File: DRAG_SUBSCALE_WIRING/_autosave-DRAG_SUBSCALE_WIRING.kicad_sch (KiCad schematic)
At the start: 7 parts, among them J1 Screw_Terminal_01x02, SW1 SW_DPST_x2, U1 Teensy4.1

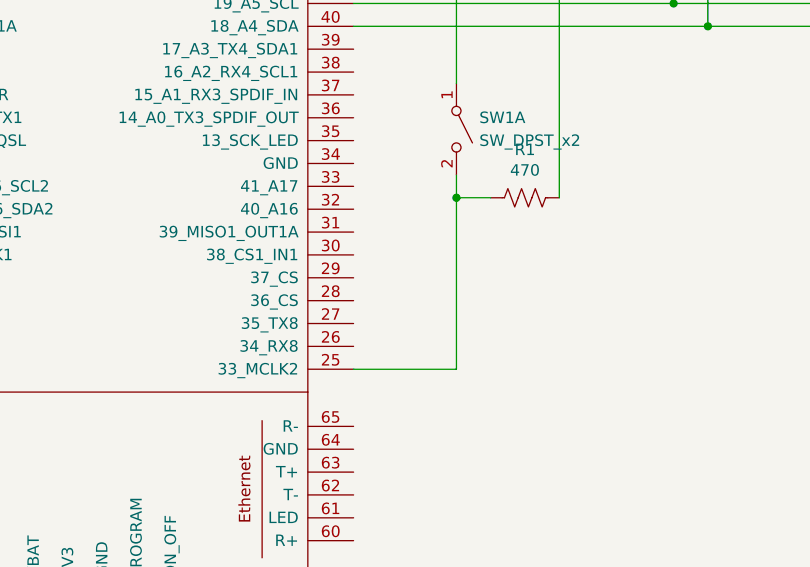
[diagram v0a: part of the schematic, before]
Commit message: Changed buzzer to be more pronounced pitch
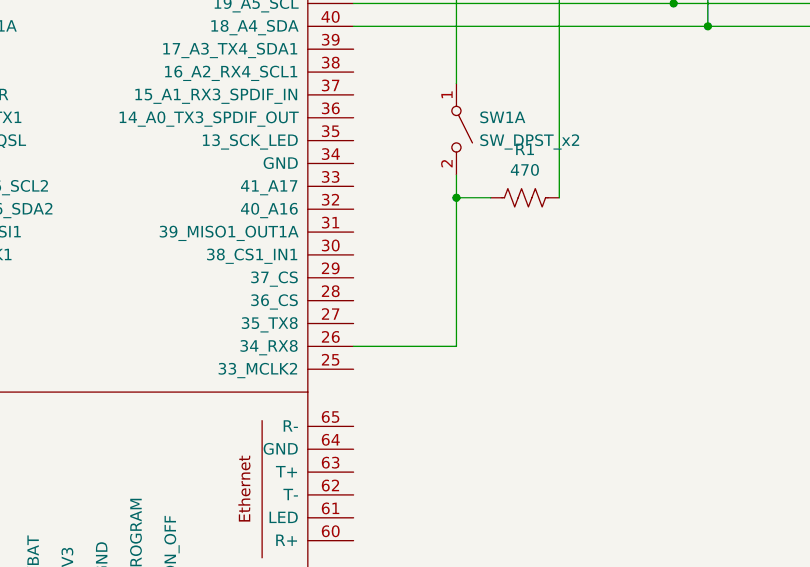
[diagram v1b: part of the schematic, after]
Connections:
- net at R1.1, SW1.2 (B): now also U1.26 (34_RX8); no longer U1.25 (33_MCLK2)
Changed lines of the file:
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@@
 	(wire
 		(pts
-			(xy 158.75 116.84) (xy 170.18 116.84)
+			(xy 158.75 114.3) (xy 170.18 114.3)
 		)
 		(stroke
@@
 	(wire
 		(pts
-			(xy 170.18 97.79) (xy 170.18 116.84)
+			(xy 170.18 97.79) (xy 170.18 114.3)
 		)
 		(stroke
